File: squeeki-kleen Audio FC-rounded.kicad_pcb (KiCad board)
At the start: 2 copper layers, 50.8 x 17.8 mm, 21 parts, among them J1 GND, J2 VCC, J3 P1, J4 P2, J5 C8, J6 GND out, U1 OPA1671IDCKT

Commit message: Art by Pickleknot
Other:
- board text added: "art: pickleknot"
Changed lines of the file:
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@@
+    (effects (font (size 0.8 0.8) (thickness 0.15)))
+  )
+  (gr_text "art: pickleknot" (at 75.565 41.275) (layer "F.SilkS")
     (effects (font (size 0.8 0.8) (thickness 0.15)))
   )

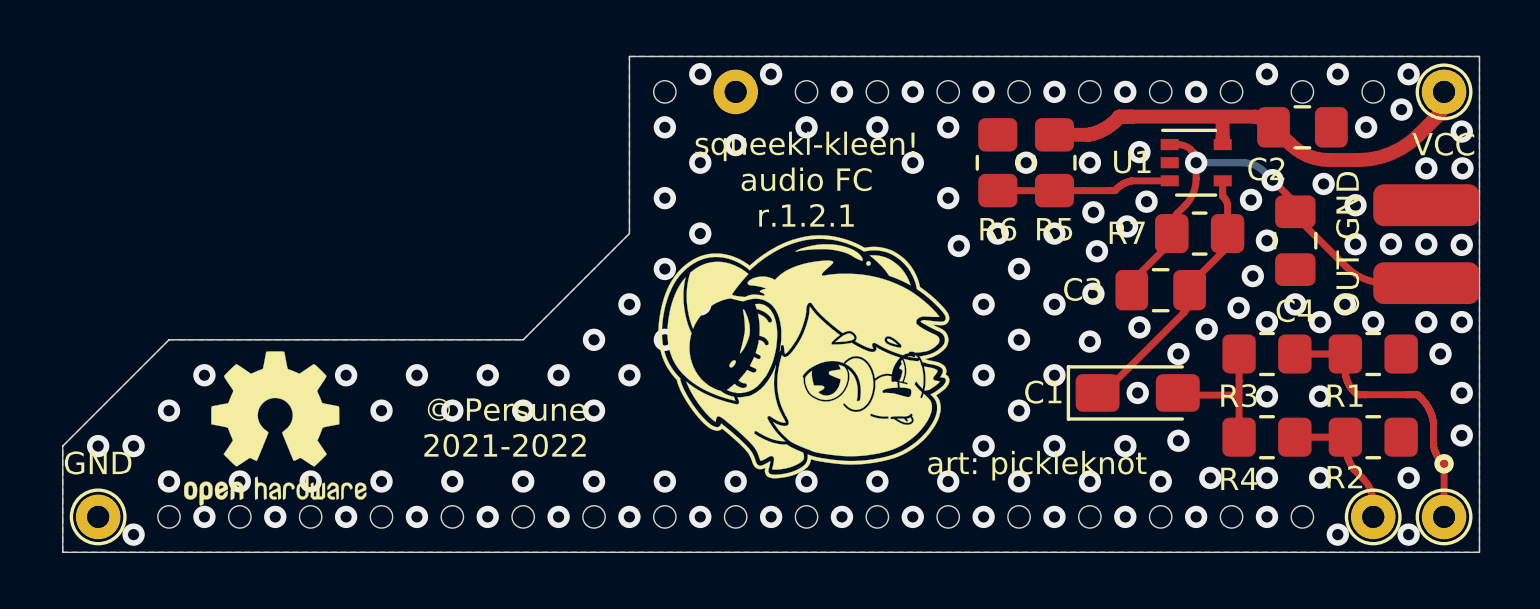
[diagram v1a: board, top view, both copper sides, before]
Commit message: Add teardrops, HTML BOM, and trace rounding
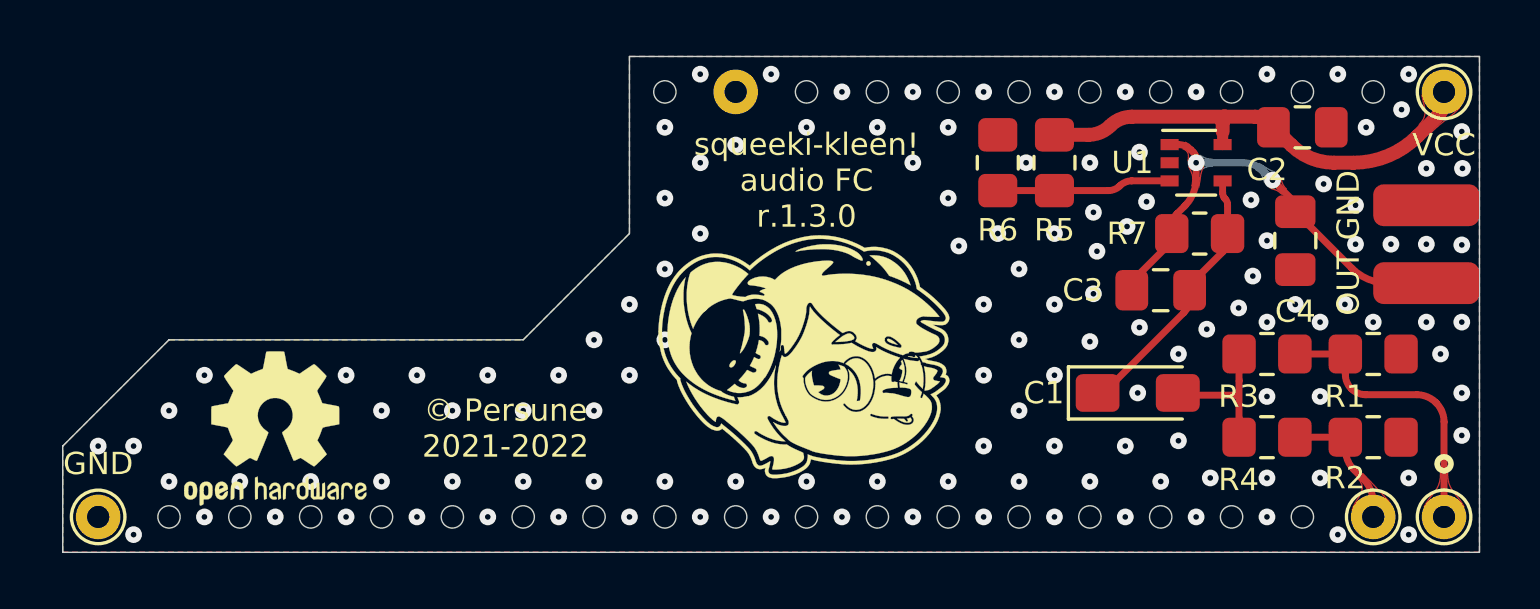
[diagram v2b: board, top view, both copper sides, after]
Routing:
- net /P1: track 13.7 -> 10.4 mm
- net VCC: track 19.8 -> 17.2 mm
- net /P2: track 6.60 -> 4.77 mm
- net Net-(R5-Pad2): track 7.22 -> 6.25 mm
- net Net-(C1-Pad1): track 10.5 -> 9.63 mm
- net /C8: track 17.3 -> 16.7 mm
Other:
- board text added: "squeeki-kleen! audio FC r.1.3.0"
- board text removed: "art: pickleknot"
- board text removed: "squeeki-kleen! audio FC r.1.2.1"
